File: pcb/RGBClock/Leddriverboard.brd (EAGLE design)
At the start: 100 x 80 mm, 37 parts, among them U1 LP3878MR-ADJ, U2 P82B96DR, U3 PCA9685PW, U4 ZXLD1362ET5TA, U5 ZXLD1362ET5TA, U6 ZXLD1362ET5TA, X1 5566-4

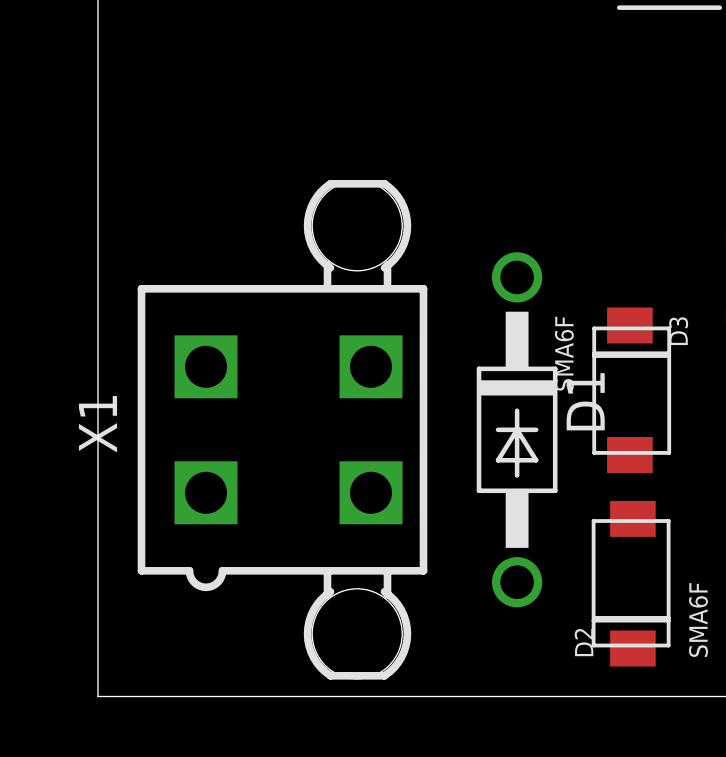
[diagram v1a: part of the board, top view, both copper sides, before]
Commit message: 
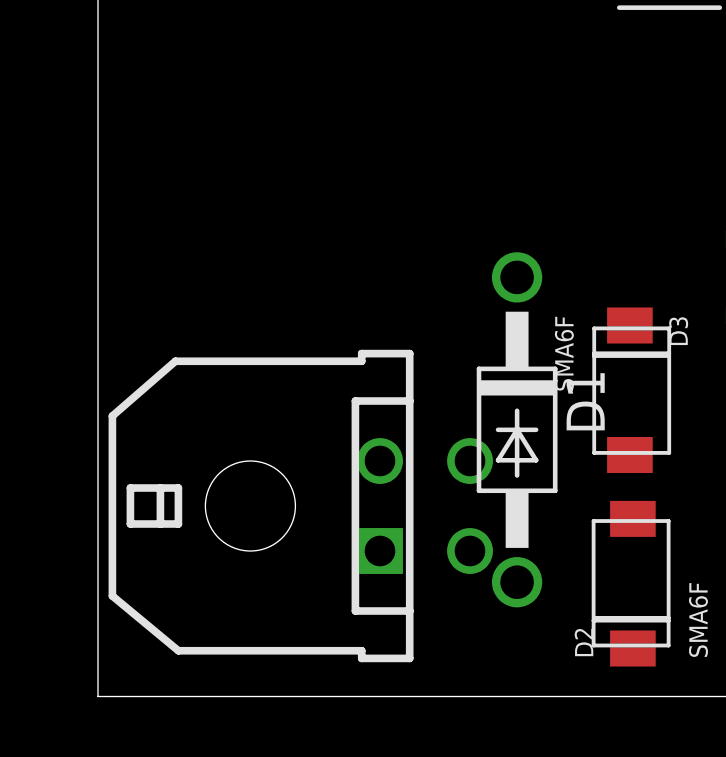
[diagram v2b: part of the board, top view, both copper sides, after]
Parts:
- removed X1: 5566-4, con-molex:5566-4
- added X3: (no value), con-molex-micro-fit-3_0:43045-0400
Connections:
- net GND: now also X3.P$1; no longer X1.3
- net N$22: now also X3.P$2; no longer X1.1
- net N$25: now also X3.P$4; no longer X1.4
- net N$7: now also X3.P$3; no longer X1.2
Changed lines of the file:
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@@
 <attribute name="OC_FARNELL" value="1576671" x="88.9" y="0" size="1.778" layer="27" display="off"/>
-</element>
-<element name="X1" library="con-molex" package="5566-4" value="5566-4" x="6.35" y="8.89" rot="R270">
-<attribute name="OC_NEWARK" value="unknown" x="-1.27" y="-33.02" size="1.778" layer="27" rot="R270" display="off"/>
-<attribute name="MPN" value="" x="-1.27" y="-33.02" size="1.778" layer="27" rot="R270" display="off"/>
-<attribute name="MF" value="" x="-1.27" y="-33.02" size="1.778" layer="27" rot="R270" display="off"/>
-<attribute name="OC_FARNELL" value="unknown" x="-1.27" y="-33.02" size="1.778" layer="27" rot="R270" display="off"/>
 </element>
 <element name="D3" library="MyComponents" package="DO-221AC" value="SMA6F" x="17.78" y="10.16" rot="R270"/>
@@
 <element name="R6" library="resistor" package="R0402" value="A1-0" x="35.56" y="12.7"/>
 <element name="R4" library="resistor" package="R0402" value="A2-0" x="35.56" y="11.43"/>
+<element name="X3" library="con-molex-micro-fit-3_0" package="43045-0400" value="" x="5.08" y="6.35" rot="R270">
+<attribute name="MATERIAL" value="" x="5.08" y="6.35" size="1.778" layer="27" rot="R270" display="off"/>
+</element>
 </elements>
 <signals>
@@
 <contactref element="D2" pad="AN"/>
 <contactref element="D3" pad="AN"/>
-<contactref element="X1" pad="3"/>
 <contactref element="U1" pad="3"/>
 <contactref element="U1" pad="9"/>
@@
 <contactref element="R9" pad="1"/>
 <contactref element="R6" pad="1"/>
+<contactref element="X3" pad="P$1"/>
 <wire x1="55.88" y1="28.3972" x2="62.1284" y2="29.21" width="0" layer="19" extent="1-1"/>
 <wire x1="62.1284" y1="17.78" x2="62.1284" y2="29.21" width="0" layer="19" extent="1-1"/>
@@
 <wire x1="17.83" y1="5.92" x2="22.9362" y2="5.715" width="0" layer="19" extent="1-1"/>
 <wire x1="17.73" y1="8.05" x2="17.83" y2="5.92" width="0" layer="19" extent="1-1"/>
-<wire x1="9.1" y1="6.79" x2="17.73" y2="8.05" width="0" layer="19" extent="1-1"/>
+<wire x1="9.4" y1="4.85" x2="17.73" y2="8.05" width="0" layer="19" extent="1-1"/>
 </signal>
 <signal name="VCC" class="2">
@@
 <contactref element="U2" pad="5"/>
 <contactref element="U2" pad="6"/>
-<contactref element="X1" pad="1"/>
 <contactref element="D2" pad="KAT"/>
+<contactref element="X3" pad="P$2"/>
 <wire x1="27.8638" y1="6.985" x2="27.8638" y2="5.715" width="0" layer="19" extent="1-1"/>
 <wire x1="17.83" y1="1.6" x2="27.8638" y2="5.715" width="0" layer="19" extent="1-1"/>
-<wire x1="3.6" y1="6.79" x2="17.83" y2="1.6" width="0" layer="19" extent="1-1"/>
+<wire x1="9.4" y1="7.85" x2="17.83" y2="1.6" width="0" layer="19" extent="1-1"/>
 </signal>
 <signal name="N$7">
 <contactref element="U2" pad="3"/>
 <contactref element="U2" pad="2"/>
-<contactref element="X1" pad="2"/>
 <contactref element="D3" pad="KAT"/>
+<contactref element="X3" pad="P$3"/>
 <wire x1="22.9362" y1="6.985" x2="22.9362" y2="8.255" width="0" layer="19" extent="1-1"/>
 <wire x1="17.73" y1="12.37" x2="22.9362" y2="8.255" width="0" layer="19" extent="1-1"/>
-<wire x1="3.6" y1="10.99" x2="17.73" y2="12.37" width="0" layer="19" extent="1-1"/>
+<wire x1="12.4" y1="4.85" x2="17.73" y2="12.37" width="0" layer="19" extent="1-1"/>
 </signal>
 <signal name="SDA">
@@
 <signal name="N$25">
 <contactref element="D1" pad="A"/>
-<contactref element="X1" pad="4"/>
-<wire x1="13.97" y1="3.81" x2="9.1" y2="10.99" width="0" layer="19" extent="1-1"/>
+<contactref element="X3" pad="P$4"/>
+<wire x1="12.4" y1="7.85" x2="13.97" y2="3.81" width="0" layer="19" extent="1-1"/>
 </signal>
 <signal name="N$41">

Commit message: 
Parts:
- X2: value (none) -> 43045-0600
- X3: value (none) -> 43045-0400
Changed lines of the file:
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@@
 <element name="R10" library="rcl" package="0204/7" value="3300" x="25.4" y="12.7"/>
 <element name="R7" library="rcl" package="0204/7" value="3300" x="25.4" y="15.24"/>
-<element name="X2" library="con-molex-micro-fit-3_0" package="43045-0600" value="" x="93.98" y="17.78" rot="R90"/>
+<element name="X2" library="con-molex-micro-fit-3_0" package="43045-0600" value="43045-0600" x="93.98" y="17.78" rot="R90"/>
 <element name="D4" library="MyComponents" package="DO-214AB" value="VS-30BQ100PBF" x="57.15" y="24.13"/>
 <element name="D5" library="MyComponents" package="DO-214AB" value="VS-30BQ100PBF" x="57.15" y="35.56"/>
@@
 <element name="R6" library="resistor" package="R0402" value="A1-0" x="35.56" y="12.7"/>
 <element name="R4" library="resistor" package="R0402" value="A2-0" x="35.56" y="11.43"/>
-<element name="X3" library="con-molex-micro-fit-3_0" package="43045-0400" value="" x="5.08" y="6.35" rot="R270">
+<element name="X3" library="con-molex-micro-fit-3_0" package="43045-0400" value="43045-0400" x="5.08" y="6.35" rot="R270">
 <attribute name="MATERIAL" value="" x="5.08" y="6.35" size="1.778" layer="27" rot="R270" display="off"/>
 </element>

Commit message: Cleanup schematic
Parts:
- renumbered X3 to X1
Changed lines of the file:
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@@
 <element name="R6" library="resistor" package="R0402" value="A1-0" x="35.56" y="12.7"/>
 <element name="R4" library="resistor" package="R0402" value="A2-0" x="35.56" y="11.43"/>
-<element name="X3" library="con-molex-micro-fit-3_0" package="43045-0400" value="43045-0400" x="5.08" y="6.35" rot="R270">
+<element name="X1" library="con-molex-micro-fit-3_0" package="43045-0400" value="43045-0400" x="5.08" y="6.35" rot="R270">
 <attribute name="MATERIAL" value="" x="5.08" y="6.35" size="1.778" layer="27" rot="R270" display="off"/>
 </element>
@@
 <contactref element="R9" pad="1"/>
 <contactref element="R6" pad="1"/>
-<contactref element="X3" pad="P$1"/>
+<contactref element="X1" pad="P$1"/>
 <wire x1="55.88" y1="28.3972" x2="62.1284" y2="29.21" width="0" layer="19" extent="1-1"/>
 <wire x1="62.1284" y1="17.78" x2="62.1284" y2="29.21" width="0" layer="19" extent="1-1"/>
@@
 <contactref element="U2" pad="6"/>
 <contactref element="D2" pad="KAT"/>
-<contactref element="X3" pad="P$2"/>
+<contactref element="X1" pad="P$2"/>
 <wire x1="27.8638" y1="6.985" x2="27.8638" y2="5.715" width="0" layer="19" extent="1-1"/>
 <wire x1="17.83" y1="1.6" x2="27.8638" y2="5.715" width="0" layer="19" extent="1-1"/>
@@
 <contactref element="U2" pad="2"/>
 <contactref element="D3" pad="KAT"/>
-<contactref element="X3" pad="P$3"/>
+<contactref element="X1" pad="P$3"/>
 <wire x1="22.9362" y1="6.985" x2="22.9362" y2="8.255" width="0" layer="19" extent="1-1"/>
 <wire x1="17.73" y1="12.37" x2="22.9362" y2="8.255" width="0" layer="19" extent="1-1"/>
@@
 <signal name="N$25">
 <contactref element="D1" pad="A"/>
-<contactref element="X3" pad="P$4"/>
+<contactref element="X1" pad="P$4"/>
 <wire x1="12.4" y1="7.85" x2="13.97" y2="3.81" width="0" layer="19" extent="1-1"/>
 </signal>

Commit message: Led driver
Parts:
- moved U3 31.8 mm to (20.3, 24.1)
- moved X2 29.2 mm to (64.8, 19.1)
- moved L1 28.0 mm to (48.3, 19.1)
- moved L2 28.0 mm to (48.3, 30.5)
- moved L3 28.0 mm to (48.3, 7.62)
- moved R11 28.0 mm to (39.4, 19.1)
- moved R12 28.0 mm to (39.4, 30.5)
- moved R13 28.0 mm to (39.4, 6.35)
- moved C5 28.0 mm to (27.9, 19.1)
- moved C6 28.0 mm to (27.9, 30.5)
- moved D6 28.0 mm to (30.5, 11.4)
- moved C7 28.0 mm to (29.2, 6.35)
- moved D4 28.0 mm to (29.2, 25.4)
- moved D5 28.0 mm to (29.2, 36.8)
- moved U4 28.0 mm to (35.6, 19.1)
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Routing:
- net GND: track 0.00 -> 153.7 mm, vias 0 -> 2
- net VCC: track 0.00 -> 135.1 mm, vias 0 -> 1
- net +5V: track 0.00 -> 48.1 mm
- net SCL: track 0.00 -> 31.5 mm, vias 0 -> 2
- net N$4: track 0.00 -> 30.3 mm, vias 0 -> 1
- net N$22: track 0.00 -> 29.3 mm, vias 0 -> 2
- net N$1: track 0.00 -> 27.4 mm, vias 0 -> 1
- net N$16: track 0.00 -> 26.2 mm, vias 0 -> 1
- net N$19: track 0.00 -> 22.9 mm
- net N$8: track 0.00 -> 22.3 mm, vias 0 -> 2
- net N$10: track 0.00 -> 20.6 mm, vias 0 -> 2
- net N$9: track 0.00 -> 20.3 mm, vias 0 -> 2
- net N$24: track 0.00 -> 20.2 mm, vias 0 -> 3
- net N$2: track 0.00 -> 19.3 mm, vias 0 -> 2
- net N$43: track 0.00 -> 11.2 mm, vias 0 -> 2
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
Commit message: Export Gerber
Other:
- board size 100 x 80 mm -> 68 x 41 mm
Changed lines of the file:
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@@
 <layer number="43" name="vRestrict" color="2" fill="10" visible="yes" active="yes"/>
 <layer number="44" name="Drills" color="7" fill="1" visible="no" active="yes"/>
-<layer number="45" name="Holes" color="7" fill="1" visible="no" active="yes"/>
+<layer number="45" name="Holes" color="7" fill="1" visible="yes" active="yes"/>
 <layer number="46" name="Milling" color="3" fill="1" visible="no" active="yes"/>
-<layer number="47" name="Measures" color="7" fill="1" visible="no" active="yes"/>
+<layer number="47" name="Measures" color="7" fill="1" visible="yes" active="yes"/>
 <layer number="48" name="Document" color="7" fill="1" visible="yes" active="yes"/>
 <layer number="49" name="Reference" color="7" fill="1" visible="yes" active="yes"/>
@@
 <board>
 <plain>
-<wire x1="0" y1="0" x2="100" y2="0" width="0" layer="20"/>
-<wire x1="100" y1="0" x2="100" y2="80" width="0" layer="20"/>
-<wire x1="100" y1="80" x2="0" y2="80" width="0" layer="20"/>
-<wire x1="0" y1="80" x2="0" y2="0" width="0" layer="20"/>
-<dimension x1="0" y1="0" x2="68.58" y2="0" x3="34.29" y3="-3.81" textsize="1.778" layer="1"/>
+<wire x1="0" y1="0" x2="68" y2="0" width="0" layer="20"/>
+<wire x1="68" y1="0" x2="68" y2="41" width="0" layer="20"/>
+<wire x1="68" y1="41" x2="0" y2="41" width="0" layer="20"/>
+<wire x1="0" y1="41" x2="0" y2="0" width="0" layer="20"/>
+<hole x="3" y="38" drill="3.2"/>
+<hole x="65" y="38" drill="3.2"/>
+<hole x="65" y="3" drill="3.2"/>
+<hole x="3" y="3" drill="3.2"/>
 </plain>
 <attributes>

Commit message: Beta version master pcb (not complete routed !)
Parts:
- moved C7 1.00 mm to (28.2, 6.35)
- moved D1 1.00 mm to (7.62, 18.8)
- moved D6 1.00 mm to (29.5, 11.4)
- moved R1 0.94 mm to (13.0, 29.3), turned to 0 degrees
- moved R3 0.50 mm to (22.1, 31.8)
- moved R5 0.50 mm to (22.1, 33.0)
- moved R8 0.50 mm to (22.1, 34.3)
- moved R2 0.23 mm to (9.11, 29.3), turned to 180 degrees
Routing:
- net GND: track 153.7 -> 0.37 mm, vias 2 -> 0
- net VCC: track 135.1 -> 121.6 mm, vias 1 -> 0
- net N$19: track 22.9 -> 13.5 mm
- net N$22: track 29.3 -> 20.8 mm, vias 2 -> 0
- net N$24: track 20.2 -> 15.9 mm, vias 3 -> 2
- net N$8: track 22.3 -> 20.2 mm
- net +5V: track 48.1 -> 50.0 mm
- net N$4: track 30.3 -> 31.7 mm, vias 1 -> 2
- net N$25: track 4.97 -> 5.97 mm
- net N$1: track 27.4 -> 26.6 mm, vias 1 -> 0
- net N$42: track 2.64 -> 3.14 mm
- added copper zone on layer 1, net GND
- added copper zone on layer 16, net GND
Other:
- board size 68 x 41 mm -> 70 x 41 mm

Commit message: Just before freerouter
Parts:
- moved C5 26.7 mm to (52.1, 30.5)
- moved U4 22.8 mm to (55.2, 30.5), turned to 90 degrees
- moved R11 21.6 mm to (55.2, 33.7), turned to 180 degrees
- moved C6 18.5 mm to (44.5, 38.7), turned to 0 degrees
- moved D4 16.5 mm to (45.1, 29.8)
- moved R9 15.4 mm to (31.1, 41.9), turned to 270 degrees
- moved U3 15.3 mm to (19.7, 39.4), turned to 180 degrees
- moved R6 15.0 mm to (29.8, 41.9), turned to 270 degrees
- moved R4 14.8 mm to (28.6, 41.9), turned to 270 degrees
- moved D6 14.5 mm to (43.8, 9.53)
- moved L2 14.4 mm to (57.8, 41.3)
- moved D5 12.3 mm to (39.4, 43.8)
- moved C7 10.5 mm to (38.7, 6.35), turned to 0 degrees
- moved R12 10.2 mm to (48.3, 35.6)
- moved U5 10.2 mm to (44.5, 35.6)
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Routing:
- net VCC: track 121.6 -> 0.00 mm
- net +5V: track 50.0 -> 0.00 mm
- net SCL: track 31.8 -> 0.00 mm, vias 2 -> 0
- net N$4: track 31.7 -> 0.00 mm, vias 2 -> 0
- net N$1: track 26.6 -> 0.00 mm
- net N$16: track 26.6 -> 0.00 mm, vias 1 -> 0
- net N$22: track 20.8 -> 0.00 mm
- net N$10: track 20.6 -> 0.00 mm, vias 2 -> 0
- net N$9: track 20.3 -> 0.00 mm, vias 2 -> 0
- net N$8: track 20.2 -> 0.00 mm, vias 2 -> 0
- net N$2: track 18.9 -> 0.00 mm, vias 2 -> 0
- net N$24: track 15.9 -> 0.00 mm, vias 2 -> 0
- net N$19: track 13.5 -> 0.00 mm
- net N$43: track 10.9 -> 0.00 mm, vias 2 -> 0
- net N$41: track 10.5 -> 0.00 mm, vias 2 -> 0
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- removed copper zone on layer 1, net GND
- removed copper zone on layer 16, net GND
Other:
- board size 70 x 41 mm -> 70 x 47.5 mm
